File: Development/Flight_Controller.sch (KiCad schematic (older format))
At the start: 231 parts, among them J1 POWER1, J2 POWER2, J3 USB_C_Receptacle, J4 Micro_SD_Card_Det, U1 MIC5330-SPYML, U10 STM32F765IIT6, U11 SN74LVC8T245, U12 TXS0108EPW, U13 NUF2042XV6T1G, U14 TXS0108EPW, U15 FM25V02-G, U16 TJA1051TK-3, U17 TJA1051TK-3, U18 TXS0108EPW, U19 SERVO_THING, U2 ICM20689, U3 MIC5330-SSYML, U4 MIC5330-SSYML, U5 MS5611-01BA, U6 BMI088, U7 IST8310, U8 EG5350CT, U9 TPS3808, Y1 Crystal, Y2 Crystal

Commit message: + New Footprints, Started PCB
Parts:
- C1, C10, C11, C12, C13, C14, C15, C16, C17, C18, C19, C2, C20, C21, C22, C23, C24, C25, C26, C27, C28, C29, C3, C30, C31, C32, C33, C34, C35, C36, C37, C38, C39, C4, C40, C41, C46, C47, C48, C49, C5, C50, C56, C57, C6, C62, C63, C64, C65, C66, C67, C68, C69, C7, C70, C71, C72, C73, C74, C75, C76, C77, C78, C79, C8, C80, C81, C9: footprint (none) -> Capacitor_SMD:C_0402_1005Metric
- L1: footprint (none) -> Inductor_SMD:L_0402_1005Metric
- R1, R10, R100, R101, R102, R103, R11, R12, R13, R14, R15, R16, R17, R18, R19, R2, R20, R21, R22, R23, R24, R25, R26, R27, R28, R29, R3, R30, R31, R32, R33, R34, R35, R36, R37, R38, R39, R4, R40, R41, R42, R43, R44, R45, R46, R47, R48, R49, R5, R50, R51, R52, R53, R54, R55, R56, R57, R58, R59, R6, R60, R61, R62, R63, R64, R65, R66, R67, R68, R69, R7, R70, R71, R72, R73, R74, R75, R76, R77, R78, R79, R8, R80, R81, R82, R83, R84, R85, R86, R87, R88, R89, R9, R90, R91, R92, R93, R94, R95, R96, R97, R98, R99: footprint (none) -> Resistor_SMD:R_0402_1005Metric

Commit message: footprint update
Found in Newfootprint folder
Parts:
- removed J1: POWER1, symbol Connector_Generic:Conn_01x06
- removed J2: POWER2, symbol Connector_Generic:Conn_01x06
- added C82: POWER1, Newfootprint:5033950610, symbol Flight_Controller-rescue:Conn_6_1-flightController
- added C83: POWER2, Newfootprint:5033950610, symbol Flight_Controller-rescue:Conn_6_1-flightController
- C42: footprint (none) -> Connectors_JST:JST_GH_BM05B-GHS-TBT_05x1.25mm_Straight
- C43: footprint (none) -> Connectors_JST:JST_GH_BM10B-GHS-TBT_10x1.25mm_Straight
- C44, C51, C52, C55, C59, C60: footprint (none) -> Connectors_JST:JST_GH_BM04B-GHS-TBT_04x1.25mm_Straight
- C45, C53, C54, C61: footprint (none) -> Connectors_JST:JST_GH_BM06B-GHS-TBT_06x1.25mm_Straight
- C58: footprint (none) -> Connectors_JST:JST_GH_BM07B-GHS-TBT_07x1.25mm_Straight
- D2: symbol LED:SMLVN6RGB -> Flight_Controller-rescue:SMLVN6RGB-LED
- LC1, LC10, LC11, LC12, LC13, LC14, LC15, LC16, LC2, LC3, LC4, LC5, LC6, LC7, LC8, LC9: footprint (none) -> Newfootprint:CAP_NFM18PS105R0J3D; symbol Device:EMI_Filter_C -> Flight_Controller-rescue:EMI_Filter_C-Device
- U11: footprint (none) -> Newfootprint:SOP65P640X120-24N
- U13: footprint (none) -> Newfootprint:SOT50P160X60-6N
- U9: footprint (none) -> Newfootprint:SOT95P280X145-6N
- Y1: value Crystal -> NX3225SA12000MHZSTDCSR1

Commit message: Complete footprints
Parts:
- BT1: value Battery_Cell -> PAS414HR-VE5R; footprint (none) -> Newfootprint:UL_PAS414HRVE5R
- D3: footprint (none) -> LED_SMD:LED_0603_1608Metric
- D4: footprint (none) -> Diode_SMD:D_SOD-123
- J4: footprint (none) -> Connector_Card:microSD_HC_Hirose_DM3AT-SF-PEJM5
- R59: value 10k -> 2K
- U19: footprint (none) -> Newfootprint:PinHeader_3x13_P2.54mm_Vertical
- U8: footprint (none) -> Button_Switch_SMD:SW_SPST_EVQP7C
- Y1: value NX3225SA12000MHZSTDCSR1 -> ABS06-32.768KHZ-9-T; footprint (none) -> Newfootprint:XTAL_ABS06-32.768KHZ-9-T
- Y2: value Crystal -> Q22FA12800400; footprint (none) -> Newfootprint:Q22FA12800400
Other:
- note added: "Update ABS circuit\n"
- note added: "Update Q22FA12800400 circuit\n"
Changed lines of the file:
@@
 F 0 "U8" H 7425 2500 50  0000 C CNN
 F 1 "EG5350CT" H 7425 2409 50  0000 C CNN
-F 2 "" H 7425 2175 50  0001 C CNN
+F 2 "Button_Switch_SMD:SW_SPST_EVQP7C" H 7425 2175 50  0001 C CNN
 F 3 "" H 7425 2175 50  0001 C CNN
 	1    7425 2175
@@
 P 14600 7950
 F 0 "Y1" H 14600 8218 50  0000 C CNN
-F 1 "NX3225SA12000MHZSTDCSR1" H 14600 8127 50  0000 C CNN
-F 2 "" H 14600 7950 50  0001 C CNN
+F 1 "ABS06-32.768KHZ-9-T" H 14600 8127 50  0000 C CNN
+F 2 "Newfootprint:XTAL_ABS06-32.768KHZ-9-T" H 14600 7950 50  0001 C CNN
 F 3 "~" H 14600 7950 50  0001 C CNN
 	1    14600 7950
@@
 F 0 "D4" H 29900 3634 50  0000 C CNN
 F 1 "D240L" H 29900 3725 50  0000 C CNN
-F 2 "" H 29900 3850 50  0001 C CNN
+F 2 "Diode_SMD:D_SOD-123" H 29900 3850 50  0001 C CNN
 F 3 "~" H 29900 3850 50  0001 C CNN
 	1    29900 3850
@@
 F 0 "U19" H 31612 5646 50  0000 R CNN
 F 1 "SERVO_THING" H 31612 5555 50  0000 R CNN
-F 2 "" H 31800 6000 50  0001 C CNN
+F 2 "Newfootprint:PinHeader_3x13_P2.54mm_Vertical" H 31800 6000 50  0001 C CNN
 F 3 "" H 31800 6000 50  0001 C CNN
 	1    31800 6000
@@
 F 0 "J4" H 26750 14867 50  0000 C CNN
 F 1 "Micro_SD_Card_Det" H 26750 14776 50  0000 C CNN
-F 2 "" H 28850 14750 50  0001 C CNN
+F 2 "Connector_Card:microSD_HC_Hirose_DM3AT-SF-PEJM5" H 28850 14750 50  0001 C CNN
 F 3 "https://au.rs-online.com/web/p/memory-sim-card-connectors/8281881/" H 26800 14150 50  0001 C CNN
 	1    26800 14050
@@
 F 0 "D3" H 28650 11235 50  0000 C CNN
 F 1 "DIODE" H 28650 11326 50  0000 C CNN
-F 2 "" H 28650 11500 50  0001 C CNN
+F 2 "LED_SMD:LED_0603_1608Metric" H 28650 11500 50  0001 C CNN
 F 3 "~" H 28650 11500 50  0001 C CNN
 	1    28650 11500
@@
 P 28200 11500
 F 0 "R59" V 28200 11550 50  0000 C CNN
-F 1 "10k" V 28200 11450 50  0000 C CNN
+F 1 "2K" V 28200 11450 50  0000 C CNN
 F 2 "Resistor_SMD:R_0402_1005Metric" H 28200 11500 50  0001 C CNN
 F 3 "~" H 28200 11500 50  0001 C CNN
@@
 P 22350 9550
 F 0 "Y2" H 22350 9818 50  0000 C CNN
-F 1 "Crystal" H 22350 9727 50  0000 C CNN
-F 2 "" H 22350 9550 50  0001 C CNN
+F 1 "Q22FA12800400" H 22350 9727 50  0000 C CNN
+F 2 "Newfootprint:Q22FA12800400" H 22350 9550 50  0001 C CNN
 F 3 "~" H 22350 9550 50  0001 C CNN
 	1    22350 9550
@@
 Wire Wire Line
 	21950 9800 22350 9800
-$Comp
-L Device:Battery_Cell BT1
-U 1 1 5D7BC7CC
-P 7600 3400
-F 0 "BT1" H 7482 3496 50  0000 R CNN
-F 1 "Battery_Cell" H 7482 3405 50  0000 R CNN
-F 2 "" V 7600 3460 50  0001 C CNN
-F 3 "~" V 7600 3460 50  0001 C CNN
-	1    7600 3400
-	-1   0    0    -1
-$EndComp
-Wire Wire Line
-	7600 3500 7600 3550
-Wire Wire Line
-	7450 3100 7600 3100
-Wire Wire Line
-	7600 3200 7600 3100
-Connection ~ 7600 3100
-Wire Wire Line
-	7600 3100 7750 3100
 NoConn ~ 16800 5500
 NoConn ~ 16800 5800
@@
 	1    0    0    -1
 $EndComp
+$Comp
+L Device:Battery_Cell BT1
+U 1 1 5D7BC7CC
+P 7600 3400
+F 0 "BT1" H 7482 3496 50  0000 R CNN
+F 1 "PAS414HR-VE5R" H 7482 3405 50  0000 R CNN
+F 2 "Newfootprint:UL_PAS414HRVE5R" V 7600 3460 50  0001 C CNN
+F 3 "~" V 7600 3460 50  0001 C CNN
+	1    7600 3400
+	-1   0    0    -1
+$EndComp
+Wire Wire Line
+	7450 3100 7600 3100
+Wire Wire Line
+	7600 3200 7600 3100
+Connection ~ 7600 3100
+Wire Wire Line
+	7600 3100 7750 3100
+Wire Wire Line
+	7600 3500 7600 3550
+Text Notes 23450 9525 0    197  ~ 0
+Update Q22FA12800400 circuit\n
+Text Notes 10675 8025 0    197  ~ 0
+Update ABS circuit\n
 $EndSCHEMATC

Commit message: PCB Started
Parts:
- removed D1: 1N5822, Diode_THT:D_DO-201AD_P15.24mm_Horizontal, symbol Diode:1N5822
- removed U19: SERVO_THING, Newfootprint:PinHeader_3x13_P2.54mm_Vertical, symbol Flight_Controller-rescue:SERVO_THING
- added D1: 1N4148WS, Diode_SMD:D_SOD-323, symbol Diode:1N4148WS
- added J3, J4, J5: Conn_01x13_Female, Connector_PinHeader_2.54mm:PinHeader_1x13_P2.54mm_Vertical, symbol Connector:Conn_01x13_Female
- C35: renamed from C82; footprint Newfootprint:5033950610 -> Connectors_JST:JST_GH_BM06B-GHS-TBT_06x1.25mm_Straight
- C36: renamed from C83; footprint Newfootprint:5033950610 -> Connectors_JST:JST_GH_BM06B-GHS-TBT_06x1.25mm_Straight
- C44: renamed from C42; value Conn_5_1 -> DSM/SBUS RC
- C45: renamed from C43; value Conn_10_1 -> GPS
- C46: renamed from C44; value Conn_4_1 -> ADC3/5
- C47: renamed from C45; value Conn_6_1 -> DSU7
- C53: renamed from C51; value Conn_4_1 -> I2C3
- C54: renamed from C52; value Conn_4_1 -> I2C4
- C55: renamed from C53; value Conn_6_1 -> USART2
- C56: renamed from C54; value Conn_6_1 -> USART3
- C57: renamed from C55; value Conn_4_1 -> I2C2
- C60: renamed from C58; value Conn_7_1 -> SPI5
- C61: renamed from C59; value Conn_4_1 -> CAN1
- C62: renamed from C60; value Conn_4_1 -> CAN2
- C63: renamed from C61; value Conn_6_1 -> UART4
- J2: renamed from J4; symbol Connector:Micro_SD_Card_Det -> Connector:Micro_SD_Card
- R56, R57, R58: value 10k -> 3k
- R59: value 2K -> 2k
- renumbered C35 to C37, C36 to C38, C37 to C39, C38 to C40, C39 to C41, C40 to C42, C41 to C43, C46 to C48, C47 to C49, C48 to C50, C49 to C51, C50 to C52, C56 to C58, C57 to C59, C62 to C64, C63 to C65, C64 to C66, C65 to C67, C66 to C68, C67 to C69, C68 to C70, C69 to C71, C70 to C72, C71 to C73, C72 to C74, C73 to C75, C74 to C76, C75 to C77, C76 to C78, C77 to C79, C78 to C80, C79 to C81, C80 to C82, C81 to C83, J3 to J1
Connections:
- net labels removed: FMU_RESET, SDIO1_CARD_DETECT, SERVO_VCC
- wire segments 792 -> 812
- no-connect marks 79 -> 80
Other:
- note added: "External Power for Servos\n"
- note removed: "Update ABS circuit\n"
- note removed: "Update Q22FA12800400 circuit\n"
- moved on the sheet: LC16

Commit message: PCB Routing Update
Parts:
- Y2: symbol Device:Crystal -> Device:Crystal_GND24
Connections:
- net 16_MHZ_IN: now also Y2.3; no longer Y2.1
- net 16_MHZ_OUT: now also Y2.1; no longer Y2.2
- net GND: now also Y2.2, Y2.4; no longer J2.9 (SHIELD)
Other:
- moved on the sheet: J2
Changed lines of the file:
@@
 $EndComp
 $Comp
-L Flight_Controller-rescue:IST8310-Symbol_Library U7
-U 1 1 5D6799FE
-P 5950 10550
-F 0 "U7" H 6025 10915 50  0000 C CNN
-F 1 "IST8310" H 6025 10824 50  0000 C CNN
-F 2 "FLIGHTFOOT:ist8310" H 6650 10950 50  0001 C CNN
-F 3 "" H 6650 10950 50  0001 C CNN
-	1    5950 10550
-	1    0    0    -1
-$EndComp
-$Comp
 L power:GND #PWR028
 U 1 1 5D67F154
@@
 Wire Wire Line
 	19750 13450 19650 13450
-$Comp
-L MCU_ST_STM32F7:STM32F765IITx U10
-U 1 1 5D31F89E
-P 18200 8900
-AR Path="/5D31F89E" Ref="U10"  Part="1"
-AR Path="/5D3376D7/5D31F89E" Ref="U?"  Part="1"
-F 0 "U10" H 17000 4450 50  0000 R CNN
-F 1 "STM32F765IIT6" H 17450 4550 50  0000 R CNN
-F 2 "Package_QFP:LQFP-176_24x24mm_P0.5mm" H 16900 4600 50  0001 R CNN
-F 3 "http://www.st.com/st-web-ui/static/active/en/resource/technical/document/datasheet/DM00273119.pdf" H 18200 8900 50  0001 C CNN
-	1    18200 8900
-	-1   0    0    1
-$EndComp
 Wire Wire Line
 	16800 7500 16350 7500
@@
 Wire Wire Line
 	16800 6000 16350 6000
-$Comp
-L Flight_Controller-rescue:MS5611-01BA U5
-U 1 1 5D63FB8E
-P 2350 8000
-F 0 "U5" H 2475 8475 50  0000 C CNN
-F 1 "MS5611-01BA" H 2475 8384 50  0000 C CNN
-F 2 "FLIGHTFOOT:ms5611" H 1850 8500 50  0001 C CNN
-F 3 "" H 1850 8500 50  0001 C CNN
-	1    2350 8000
-	1    0    0    -1
-$EndComp
 Wire Wire Line
 	2000 7850 1850 7850
@@
 Text Label 15550 4700 0    50   ~ 0
 nVDD_5V_PERIPH_OC
-$Comp
-L power:GND #PWR072
-U 1 1 5DCE191A
-P 21850 7500
-F 0 "#PWR072" H 21850 7250 50  0001 C CNN
-F 1 "GND" H 21855 7327 50  0000 C CNN
-F 2 "" H 21850 7500 50  0001 C CNN
-F 3 "" H 21850 7500 50  0001 C CNN
-	1    21850 7500
-	0    -1   -1   0
-$EndComp
 Wire Wire Line
 	19700 5000 21950 5000
@@
 	14950 7700 14950 8100
 Wire Wire Line
-	16800 8200 14600 8200
-Wire Wire Line
 	16800 8100 14950 8100
 Text GLabel 15900 18500 2    50   Input ~ 0
@@
 $EndComp
 $Comp
-L power:GND #PWR0114
-U 1 1 62C365AC
-P 31150 1050
-F 0 "#PWR0114" H 31150 800 50  0001 C CNN
-F 1 "GND" H 31155 877 50  0000 C CNN
-F 2 "" H 31150 1050 50  0001 C CNN
-F 3 "" H 31150 1050 50  0001 C CNN
-	1    31150 1050
-	-1   0    0    1
-$EndComp
-$Comp
 L power:GND #PWR097
 U 1 1 62CD7879
@@
 L Connector:Micro_SD_Card J2
 U 1 1 5D7070DE
-P 26800 13950
-F 0 "J2" H 26750 14767 50  0000 C CNN
-F 1 "Micro_SD_Card_Det" H 26750 14676 50  0000 C CNN
-F 2 "Connector_Card:microSD_HC_Hirose_DM3AT-SF-PEJM5" H 28850 14650 50  0001 C CNN
-F 3 "https://au.rs-online.com/web/p/memory-sim-card-connectors/8281881/" H 26800 14050 50  0001 C CNN
-	1    26800 13950
+P 26775 13950
+F 0 "J2" H 26725 14767 50  0000 C CNN
+F 1 "Micro_SD_Card_Det" H 26725 14676 50  0000 C CNN
+F 2 "Connector_Card:microSD_HC_Hirose_DM3AT-SF-PEJM5" H 28825 14650 50  0001 C CNN
+F 3 "https://au.rs-online.com/web/p/memory-sim-card-connectors/8281881/" H 26775 14050 50  0001 C CNN
+	1    26775 13950
 	1    0    0    -1
 $EndComp
@@
 SDMMC1_CMD
 Wire Wire Line
-	25500 13650 25900 13650
+	25500 13650 25875 13650
 Wire Wire Line
-	25900 13750 25500 13750
+	25900 13750 25875 13750
 Wire Wire Line
-	25500 13850 25900 13850
+	25500 13850 25875 13850
 Text GLabel 25500 14050 0    50   Input ~ 0
 SDMMC1_CLK
 Wire Wire Line
-	25500 14050 25900 14050
+	25500 14050 25875 14050
 Text GLabel 25500 14250 0    50   Input ~ 0
 SDMMC1_D0
@@
 SDMMC1_D1
 Wire Wire Line
-	25500 14350 25900 14350
+	25500 14350 25875 14350
 Wire Wire Line
-	25500 14250 25900 14250
+	25500 14250 25875 14250
 $Comp
 L power:GND #PWR084
@@
 $EndComp
 Wire Wire Line
-	25800 14150 25900 14150
+	25800 14150 25875 14150
 $Comp
 L power:GND #PWR082
@@
 	24600 14000 24600 13950
 Wire Wire Line
-	24600 13950 25900 13950
+	24600 13950 25875 13950
 Text GLabel 24600 13800 1    50   Input ~ 0
 TF_3V3
@@
 Text GLabel 27950 10750 0    50   Input ~ 0
 nLED_GREEN
-$Comp
-L pspice:DIODE D3
-U 1 1 5D70AE62
-P 28650 11500
-F 0 "D3" H 28650 11235 50  0000 C CNN
-F 1 "DIODE" H 28650 11326 50  0000 C CNN
-F 2 "LED_SMD:LED_0603_1608Metric" H 28650 11500 50  0001 C CNN
-F 3 "~" H 28650 11500 50  0001 C CNN
-	1    28650 11500
-	-1   0    0    1
-$EndComp
 Wire Wire Line
 	29050 10950 29050 10750
@@
 $EndComp
 $Comp
-L Device:Crystal Y2
+L Device:Crystal_GND24 Y2
 U 1 1 628F47A2
 P 22350 9550
@@
 F 3 "~" H 22350 9550 50  0001 C CNN
 	1    22350 9550
-	0    -1   -1   0
+	0    1    1    0
 $EndComp
 Wire Wire Line
@@
 	1    0    0    -1
 $EndComp
+Wire Wire Line
+	16800 8200 14600 8200
+$Comp
+L MCU_ST_STM32F7:STM32F765IITx U10
+U 1 1 5D31F89E
+P 18200 8900
+AR Path="/5D31F89E" Ref="U10"  Part="1"
+AR Path="/5D3376D7/5D31F89E" Ref="U?"  Part="1"
+F 0 "U10" H 17000 4450 50  0000 R CNN
+F 1 "STM32F765IIT6" H 17450 4550 50  0000 R CNN
+F 2 "Package_QFP:LQFP-176_24x24mm_P0.5mm" H 16900 4600 50  0001 R CNN
+F 3 "http://www.st.com/st-web-ui/static/active/en/resource/technical/document/datasheet/DM00273119.pdf" H 18200 8900 50  0001 C CNN
+	1    18200 8900
+	-1   0    0    1
+$EndComp
+$Comp
+L power:GND #PWR072
+U 1 1 5DCE191A
+P 21850 7500
+F 0 "#PWR072" H 21850 7250 50  0001 C CNN
+F 1 "GND" H 21855 7327 50  0000 C CNN
+F 2 "" H 21850 7500 50  0001 C CNN
+F 3 "" H 21850 7500 50  0001 C CNN
+	1    21850 7500
+	0    -1   -1   0
+$EndComp
+$Comp
+L power:GND #PWR0118
+U 1 1 5DA3A28E
+P 22550 9550
+F 0 "#PWR0118" H 22550 9300 50  0001 C CNN
+F 1 "GND" H 22555 9377 50  0000 C CNN
+F 2 "" H 22550 9550 50  0001 C CNN
+F 3 "" H 22550 9550 50  0001 C CNN
+	1    22550 9550
+	0    -1   -1   0
+$EndComp
+$Comp
+L power:GND #PWR0119
+U 1 1 5DA3A68E
+P 22150 9550
+F 0 "#PWR0119" H 22150 9300 50  0001 C CNN
+F 1 "GND" H 22155 9377 50  0000 C CNN
+F 2 "" H 22150 9550 50  0001 C CNN
+F 3 "" H 22150 9550 50  0001 C CNN
+	1    22150 9550
+	0    1    1    0
+$EndComp
+$Comp
+L Flight_Controller-rescue:IST8310-Symbol_Library U7
+U 1 1 5D6799FE
+P 5950 10550
+F 0 "U7" H 6025 10915 50  0000 C CNN
+F 1 "IST8310" H 6025 10824 50  0000 C CNN
+F 2 "FLIGHTFOOT:ist8310" H 6650 10950 50  0001 C CNN
+F 3 "" H 6650 10950 50  0001 C CNN
+	1    5950 10550
+	1    0    0    -1
+$EndComp
+$Comp
+L pspice:DIODE D3
+U 1 1 5D70AE62
+P 28650 11500
+F 0 "D3" H 28650 11235 50  0000 C CNN
+F 1 "DIODE" H 28650 11326 50  0000 C CNN
+F 2 "LED_SMD:LED_0603_1608Metric" H 28650 11500 50  0001 C CNN
+F 3 "~" H 28650 11500 50  0001 C CNN
+	1    28650 11500
+	-1   0    0    1
+$EndComp
+Connection ~ 25875 13650
+Wire Wire Line
+	25875 13650 25900 13650
+Connection ~ 25875 13750
+Wire Wire Line
+	25875 13750 25500 13750
+Connection ~ 25875 13850
+Wire Wire Line
+	25875 13850 25900 13850
+Connection ~ 25875 13950
+Wire Wire Line
+	25875 13950 25900 13950
+Connection ~ 25875 14050
+Wire Wire Line
+	25875 14050 25900 14050
+Connection ~ 25875 14150
+Wire Wire Line
+	25875 14150 25900 14150
+Connection ~ 25875 14250
+Wire Wire Line
+	25875 14250 25900 14250
+Connection ~ 25875 14350
+Wire Wire Line
+	25875 14350 25900 14350
+$Comp
+L Flight_Controller-rescue:MS5611-01BA U5
+U 1 1 5D63FB8E
+P 2350 8000
+F 0 "U5" H 2475 8475 50  0000 C CNN
+F 1 "MS5611-01BA" H 2475 8384 50  0000 C CNN
+F 2 "FLIGHTFOOT:ms5611" H 1850 8500 50  0001 C CNN
+F 3 "" H 1850 8500 50  0001 C CNN
+	1    2350 8000
+	1    0    0    -1
+$EndComp
+$Comp
+L power:GND #PWR0114
+U 1 1 62C365AC
+P 31150 1050
+F 0 "#PWR0114" H 31150 800 50  0001 C CNN
+F 1 "GND" H 31155 877 50  0000 C CNN
+F 2 "" H 31150 1050 50  0001 C CNN
+F 3 "" H 31150 1050 50  0001 C CNN
+	1    31150 1050
+	-1   0    0    1
+$EndComp
 $EndSCHEMATC

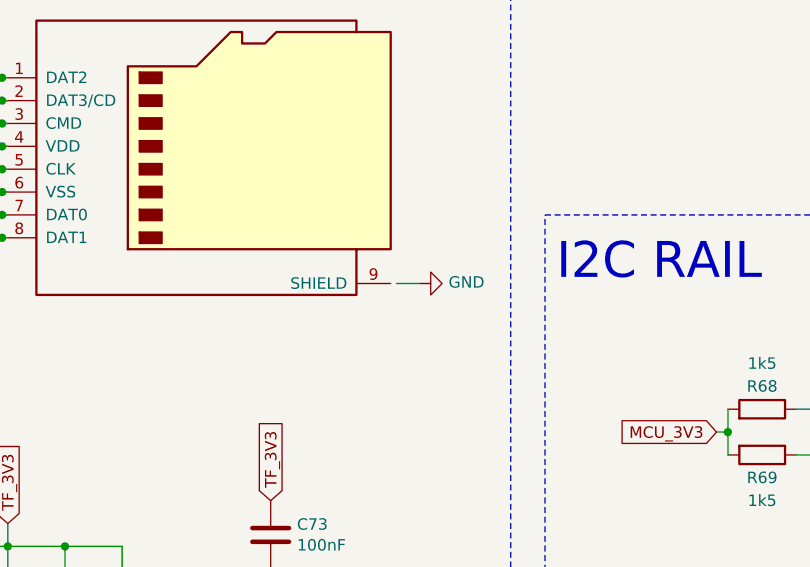
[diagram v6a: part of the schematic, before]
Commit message: PCB 4 layers, 89 unrouted
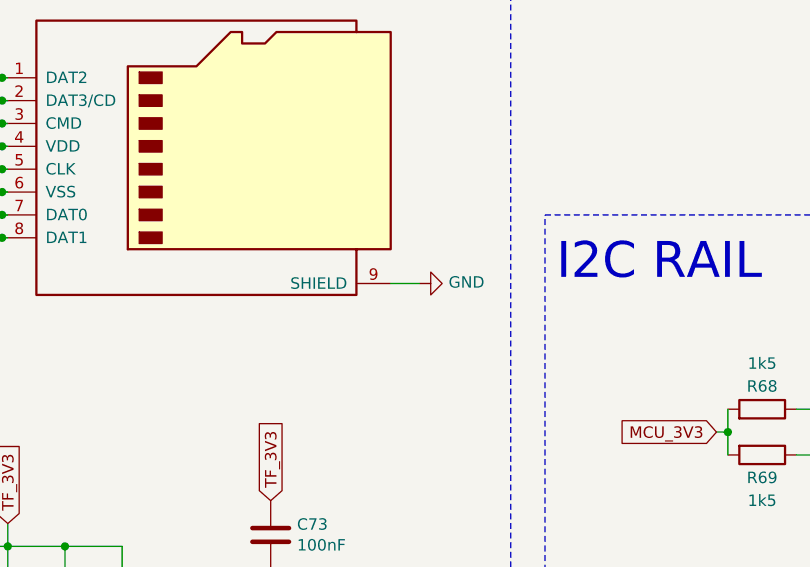
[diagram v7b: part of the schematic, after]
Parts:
- LC1, LC10, LC11, LC12, LC13, LC14, LC15, LC16, LC2, LC3, LC4, LC5, LC6, LC7, LC8, LC9: footprint Newfootprint:CAP_NFM18PS105R0J3D -> FLIGHTFOOT:FIL_NFM21PC105B1C3D
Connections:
- net GND: now also J2.9 (SHIELD)

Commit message: Updated some capacitor footprints
Updated footprints from from 0402_1005 to 0603_1608, still need to do a lot more
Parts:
- C12, C13, C18, C19, C20, C21, C22, C23, C24, C25, C7, C8, C80, C9: footprint Capacitor_SMD:C_0402_1005Metric -> Capacitor_SMD:C_0603_1608Metric
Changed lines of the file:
@@
 F 0 "C18" V 5475 2100 50  0000 C CNN
 F 1 "47uF" V 5375 2200 50  0000 C CNN
-F 2 "Capacitor_SMD:C_0402_1005Metric" H 5563 2050 50  0001 C CNN
+F 2 "Capacitor_SMD:C_0603_1608Metric" H 5563 2050 50  0001 C CNN
 F 3 "~" H 5525 2200 50  0001 C CNN
 	1    5525 2200
@@
 F 0 "C22" V 5950 2100 50  0000 C CNN
 F 1 "47uF" V 5850 2200 50  0000 C CNN
-F 2 "Capacitor_SMD:C_0402_1005Metric" H 6038 2050 50  0001 C CNN
+F 2 "Capacitor_SMD:C_0603_1608Metric" H 6038 2050 50  0001 C CNN
 F 3 "~" H 6000 2200 50  0001 C CNN
 	1    6000 2200
@@
 F 0 "C19" V 5475 3525 50  0000 C CNN
 F 1 "47uF" V 5375 3625 50  0000 C CNN
-F 2 "Capacitor_SMD:C_0402_1005Metric" H 5563 3475 50  0001 C CNN
+F 2 "Capacitor_SMD:C_0603_1608Metric" H 5563 3475 50  0001 C CNN
 F 3 "~" H 5525 3625 50  0001 C CNN
 	1    5525 3625
@@
 F 0 "C23" V 5950 3525 50  0000 C CNN
 F 1 "47uF" V 5850 3625 50  0000 C CNN
-F 2 "Capacitor_SMD:C_0402_1005Metric" H 6038 3475 50  0001 C CNN
+F 2 "Capacitor_SMD:C_0603_1608Metric" H 6038 3475 50  0001 C CNN
 F 3 "~" H 6000 3625 50  0001 C CNN
 	1    6000 3625
@@
 F 0 "C21" V 5925 4925 50  0000 C CNN
 F 1 "47uF" V 5825 5025 50  0000 C CNN
-F 2 "Capacitor_SMD:C_0402_1005Metric" H 6013 4875 50  0001 C CNN
+F 2 "Capacitor_SMD:C_0603_1608Metric" H 6013 4875 50  0001 C CNN
 F 3 "~" H 5975 5025 50  0001 C CNN
 	1    5975 5025
@@
 F 0 "C20" V 5475 4925 50  0000 C CNN
 F 1 "47uF" V 5375 5025 50  0000 C CNN
-F 2 "Capacitor_SMD:C_0402_1005Metric" H 5563 4875 50  0001 C CNN
+F 2 "Capacitor_SMD:C_0603_1608Metric" H 5563 4875 50  0001 C CNN
 F 3 "~" H 5525 5025 50  0001 C CNN
 	1    5525 5025
@@
 F 0 "C13" V 5200 2100 50  0000 C CNN
 F 1 "47uF" V 5100 2200 50  0000 C CNN
-F 2 "Capacitor_SMD:C_0402_1005Metric" H 5288 2050 50  0001 C CNN
+F 2 "Capacitor_SMD:C_0603_1608Metric" H 5288 2050 50  0001 C CNN
 F 3 "~" H 5250 2200 50  0001 C CNN
 	1    5250 2200
@@
 F 0 "C24" V 6350 2100 50  0000 C CNN
 F 1 "47uF" V 6250 2200 50  0000 C CNN
-F 2 "Capacitor_SMD:C_0402_1005Metric" H 6438 2050 50  0001 C CNN
+F 2 "Capacitor_SMD:C_0603_1608Metric" H 6438 2050 50  0001 C CNN
 F 3 "~" H 6400 2200 50  0001 C CNN
 	1    6400 2200
@@
 F 0 "C25" V 6350 4925 50  0000 C CNN
 F 1 "47uF" V 6250 5025 50  0000 C CNN
-F 2 "Capacitor_SMD:C_0402_1005Metric" H 6438 4875 50  0001 C CNN
+F 2 "Capacitor_SMD:C_0603_1608Metric" H 6438 4875 50  0001 C CNN
 F 3 "~" H 6400 5025 50  0001 C CNN
 	1    6400 5025
@@
 F 0 "C7" V 3900 2050 50  0000 C CNN
 F 1 "47uF" V 4100 1950 50  0000 C CNN
-F 2 "Capacitor_SMD:C_0402_1005Metric" H 3988 1800 50  0001 C CNN
+F 2 "Capacitor_SMD:C_0603_1608Metric" H 3988 1800 50  0001 C CNN
 F 3 "~" H 3950 1950 50  0001 C CNN
 	1    3950 1950
@@
 F 0 "C8" V 3900 3750 50  0000 C CNN
 F 1 "47uF" V 4100 3650 50  0000 C CNN
-F 2 "Capacitor_SMD:C_0402_1005Metric" H 3988 3500 50  0001 C CNN
+F 2 "Capacitor_SMD:C_0603_1608Metric" H 3988 3500 50  0001 C CNN
 F 3 "~" H 3950 3650 50  0001 C CNN
 	1    3950 3650
@@
 F 0 "C9" V 3900 5450 50  0000 C CNN
 F 1 "47uF" V 4100 5350 50  0000 C CNN
-F 2 "Capacitor_SMD:C_0402_1005Metric" H 3988 5200 50  0001 C CNN
+F 2 "Capacitor_SMD:C_0603_1608Metric" H 3988 5200 50  0001 C CNN
 F 3 "~" H 3950 5350 50  0001 C CNN
 	1    3950 5350
@@
 F 0 "C12" V 4250 5450 50  0000 C CNN
 F 1 "47uF" V 4450 5350 50  0000 C CNN
-F 2 "Capacitor_SMD:C_0402_1005Metric" H 4338 5200 50  0001 C CNN
+F 2 "Capacitor_SMD:C_0603_1608Metric" H 4338 5200 50  0001 C CNN
 F 3 "~" H 4300 5350 50  0001 C CNN
 	1    4300 5350
@@
 F 0 "C80" H 29915 11046 50  0000 L CNN
 F 1 "47uF" H 29915 10955 50  0000 L CNN
-F 2 "Capacitor_SMD:C_0402_1005Metric" H 29838 10850 50  0001 C CNN
+F 2 "Capacitor_SMD:C_0603_1608Metric" H 29838 10850 50  0001 C CNN
 F 3 "~" H 29800 11000 50  0001 C CNN
 	1    29800 11000
